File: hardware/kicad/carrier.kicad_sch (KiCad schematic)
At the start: 57 parts, among them J2 Heltec_J2, J3 Heltec_J3, U2 TCA9534PWR, U3 NS4168

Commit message: hardware: carrier hierarchical schematic; carrier_tme derives its hierarchy from carrier
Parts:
- removed C_AMP1: 100uF 6.3V, Capacitor_SMD:C_1206_3216Metric_Pad1.33x1.80mm_HandSolder, symbol Device:C
- removed C_AMP2: 1uF, Capacitor_SMD:C_0805_2012Metric_Pad1.18x1.45mm_HandSolder, symbol Device:C
- removed C_BB1, C_BR1, C_EXP1: 100nF, Capacitor_SMD:C_0805_2012Metric_Pad1.18x1.45mm_HandSolder, symbol Device:C
- removed Q_BZ1, Q_LB1, Q_LR1: BSS138, Package_TO_SOT_SMD:SOT-23, symbol Transistor_FET:BSS138
- removed R_GBZ1, R_GLB1, R_GLR1, R_SB1, R_SD1, R_SR1: 1k, Resistor_SMD:R_0805_2012Metric_Pad1.20x1.40mm_HandSolder, symbol Device:R
- removed R_INT1, R_PDBZ1, R_PDLB1, R_PDLR1, R_PUB1, R_PUR1, R_SDPD1: 10k, Resistor_SMD:R_0805_2012Metric_Pad1.20x1.40mm_HandSolder, symbol Device:R
- removed R_LLB1, R_LLR1: 0R, Resistor_SMD:R_0805_2012Metric_Pad1.20x1.40mm_HandSolder, symbol Device:R
- removed U2: TCA9534PWR, Package_SO:TSSOP-16_4.4x5mm_P0.65mm, symbol Interface_Expansion:TCA9534
- added #X_BTN_B: ONPOW LAS1-AGQ-11E/B/6V, symbol local:Button_LED_4
- added #X_BTN_R: ONPOW LAS1-AGQ-11E/R/6V, symbol local:Button_LED_4
- added #X_BUZ: BZ-38 buzzer, symbol Device:Buzzer
- added #X_HBAT: Heltec V4 battery, symbol local:Conn_W_02
- added #X_LCD: LCD 1602 + PCF8574, symbol local:Module_I2C_4
- added #X_NFC: PN532 (I2C), symbol local:Module_I2C_4
- added #X_PACK: Pack board (P5), symbol local:Pack_Link_6
- added #X_SPK: VISATON K 50, 8 ohm, symbol Device:Speaker
- J2: symbol Connector_Generic:Conn_01x18 -> local:Heltec_V4_J2
- J3: symbol Connector_Generic:Conn_01x18 -> local:Heltec_V4_J3
- J_BTN_B1, J_BTN_R1, J_LCD1, J_NFC1: symbol Connector_Generic:Conn_01x04 -> local:Conn_W_04
- J_BUZ1, J_HBAT1, J_SPK1: symbol Connector_Generic:Conn_01x02 -> local:Conn_W_02
- J_PWR1: symbol Connector_Generic:Conn_01x06 -> local:Conn_W_06
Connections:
- net +3V3: now also #X_NFC.2 (VCC)
- net +5V: now also #X_BTN_B.3 (LED+), #X_BTN_R.3 (LED+), #X_BUZ.1 (+), #X_LCD.2 (VCC), #X_PACK.4 (5V)
- net BTN_B_LEDK: now also #X_BTN_B.4 (LED-)
- net BTN_B_SW: now also #X_BTN_B.1 (SW)
- net BTN_R_LEDK: now also #X_BTN_R.4 (LED-)
- net BTN_R_SW: now also #X_BTN_R.1 (SW)
- net BUZ_K: now also #X_BUZ.2 (-)
- net GND: now also #X_BTN_B.2 (COM), #X_BTN_R.2 (COM), #X_HBAT.2, #X_LCD.1 (GND), #X_NFC.1 (GND), #X_PACK.1 (GND), #X_PACK.2 (GND)
- net SCL_3V3: now also #X_NFC.4 (SCL), #X_PACK.6 (SCL)
- net SCL_5V: now also #X_LCD.4 (SCL)
- net SDA_3V3: now also #X_NFC.3 (SDA), #X_PACK.5 (SDA)
- net SDA_5V: now also #X_LCD.3 (SDA)
- net SPK_N: now also #X_SPK.1
- net SPK_P: now also #X_SPK.2
- net VBAT_SW: now also #X_HBAT.1, #X_PACK.3 (VBAT)
- no-connect marks 26 -> 24
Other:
- added sheet GPIO expander (0x20), button inputs (carrier-expander.kicad_sch)
- added sheet Low-side drivers: button LEDs, buzzer (carrier-drivers.kicad_sch)
- added sheet NS4168 supply and shutdown (carrier-audio.kicad_sch)
- note added: "Heltec WiFi LoRa 32 V4 (plugs into J2/J3)"
- note added: "XH-2"
- note added: "XH-2 to the module's SH1.25"
- note added: "XH-2, BTL: neither side is GND"
- note added: "XH-4"
- note added: "XH-6"
- note removed: "Debug: UART, I2C, test pads"
- note removed: "GPIO expander (0x20), button inputs"
- note removed: "Heltec V4 headers"
- note removed: "I2C level shifter, LCD (5 V), NFC (3.3 V)"
- note removed: "I2S speaker amp"
- note removed: "Low-side drivers: button LEDs, buzzer"
- note removed: "Mounting holes"
- note removed: "Power in (from pack board)"
- title: AirsoftCounter v2 carrier -> AirsoftCounter v2 carrier: system
- moved on the sheet: C_5V1, C_5V2, C_BULK1, C_BULK2, C_NFC1, D_FLY1, H1, H2, H3, H4, J2, J3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

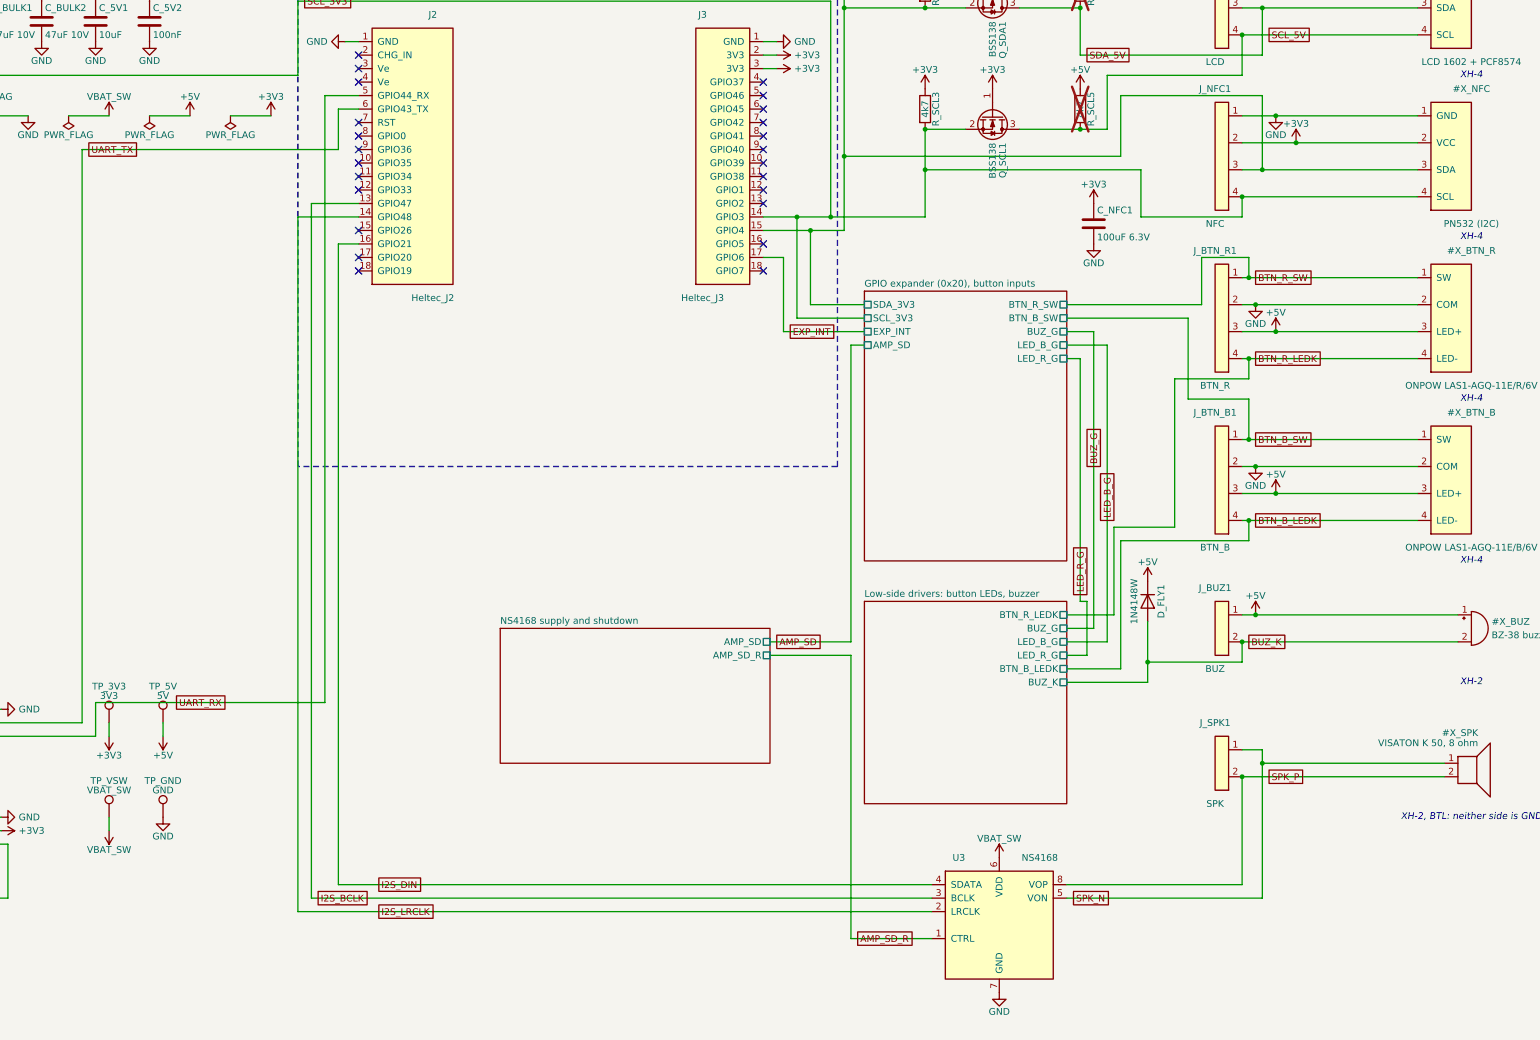
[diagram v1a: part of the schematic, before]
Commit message: hardware: carrier audio sheet draws the whole NS4168, not just its side network
The first pass put U3 on the root beside J_SPK1 and left the audio sheet with R_SD1/R_SDPD1 plus
C_AMP1/C_AMP2 only: a ~15% full A4 page that showed the audio function's side network while the amp
itself sat on the system sheet. That is the split-function failure the migration set out to remove,
and no gate catches it (ERC 0, parity 0, review 0 errors, overlaps 0 all passed).

The whole NS4168 circuit now lives on the audio sheet, laid along its signal path: I2S in on the left,
U3, SPK+/- out on the right to J_SPK1 (which stays on the root so the off-board speaker hangs off it),
AMP_SD entering at the bottom through R_SD1 with R_SDPD1 to GND, and C_AMP1/C_AMP2 beside U3's VDD.
AMP_SD_R is now internal to the sheet. carrier_tme needs no edit: it replaces BLOCKS[1] wholesale, so
U3 simply ceases to exist there and its root no longer has one to drop.

Gates: netlist matches both boards; carrier all + carrier_tme all exit 0 (ERC 0, DRC 0 violations /
0 unconnected / 0 parity, gerbers ok); pcb_diff vs 66bdf5c identical apart from footprint paths
(carrier 25/57 path-changed, carrier_tme 0/73); jlc_bom/jlc_cpl/tme_bom byte-identical; review with
board 0 errors both (5 and 6 warnings, unchanged kinds); audio page now A5 and complete.
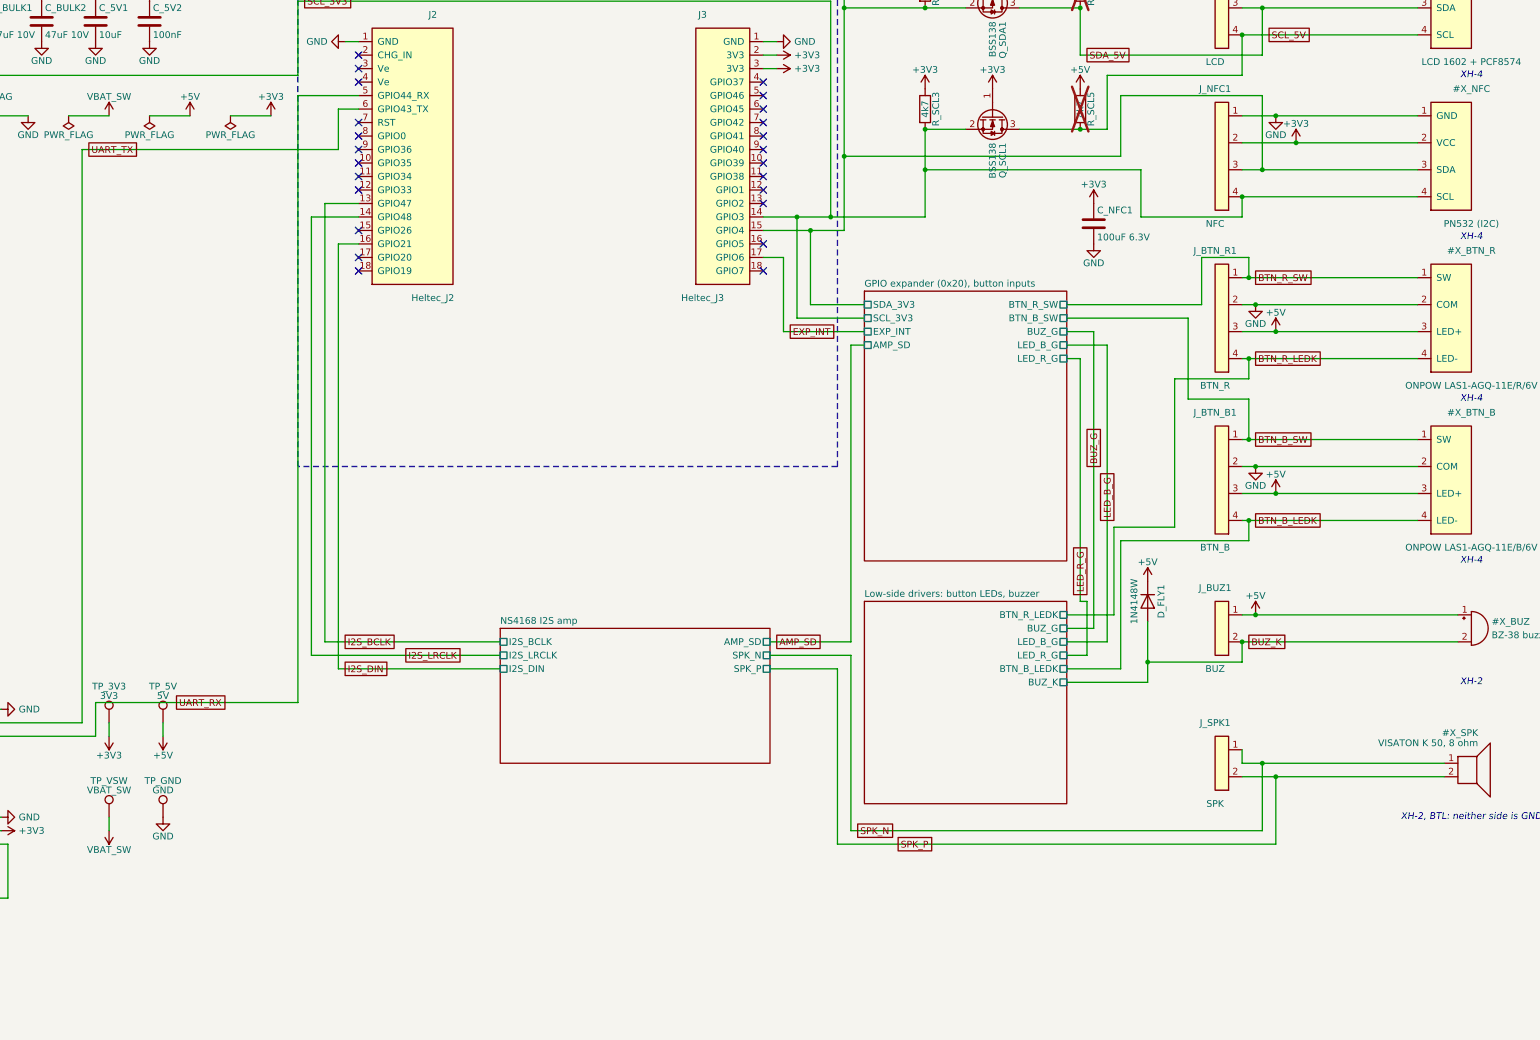
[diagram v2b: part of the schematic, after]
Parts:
- removed U3: NS4168, Package_SO:HSOP-8-1EP_3.9x4.9mm_P1.27mm_EP2.3x2.3mm_ThermalVias, symbol local:NS4168
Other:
- sheet NS4168 supply and shutdown renamed NS4168 I2S amp
- sheet NS4168 I2S amp ports: added I2S_BCLK, I2S_DIN, I2S_LRCLK, SPK_N, SPK_P; removed AMP_SD_R
